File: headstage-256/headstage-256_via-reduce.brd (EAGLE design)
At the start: 32 x 32 mm, 291 parts, among them J2 MMCX-J-P-H-ST-SM1/U.FL-R-SMT(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, J4 PINHD-2X5+4DF40-HEAD, J5 5041940270, U1 OPA170, U10 NRF24L01QFN, U11 CAT4016_QFN, U12 CAT4016_QFN, U13 TPL0501_UQFN, U14 TPL0501_UQFN, U15 MICROSD_473093751, U16 10M08SAM15317G, U17 Si8487DB, U18 MAX17048_WLP, U19 BNO055, U2 OPA170, U20 TPS61202, U21 RHD2064_BGA, U22 RHD2064_BGA, U23 TS4231, U24 TS4231, U25 LT3463, U26 ASCO-50.000MHZ-EK-T3, U27 TS4231, U28 TLV70733, U29 TS4231, U3 INA826, U30 RHD2064_BGA, U31 RHD2064_BGA, U32 MIC23150, U33 TS4231, U34 TS4231, U35 TPS8268180, U4 INA826, U5 DAC5311, U6 DAC5311, U7 DS90UB913A_WQFN, U8 ADG1401, U9 ADG1401, Y1 FW1600008, Y2 ECS-.327-12.5-1210-TR

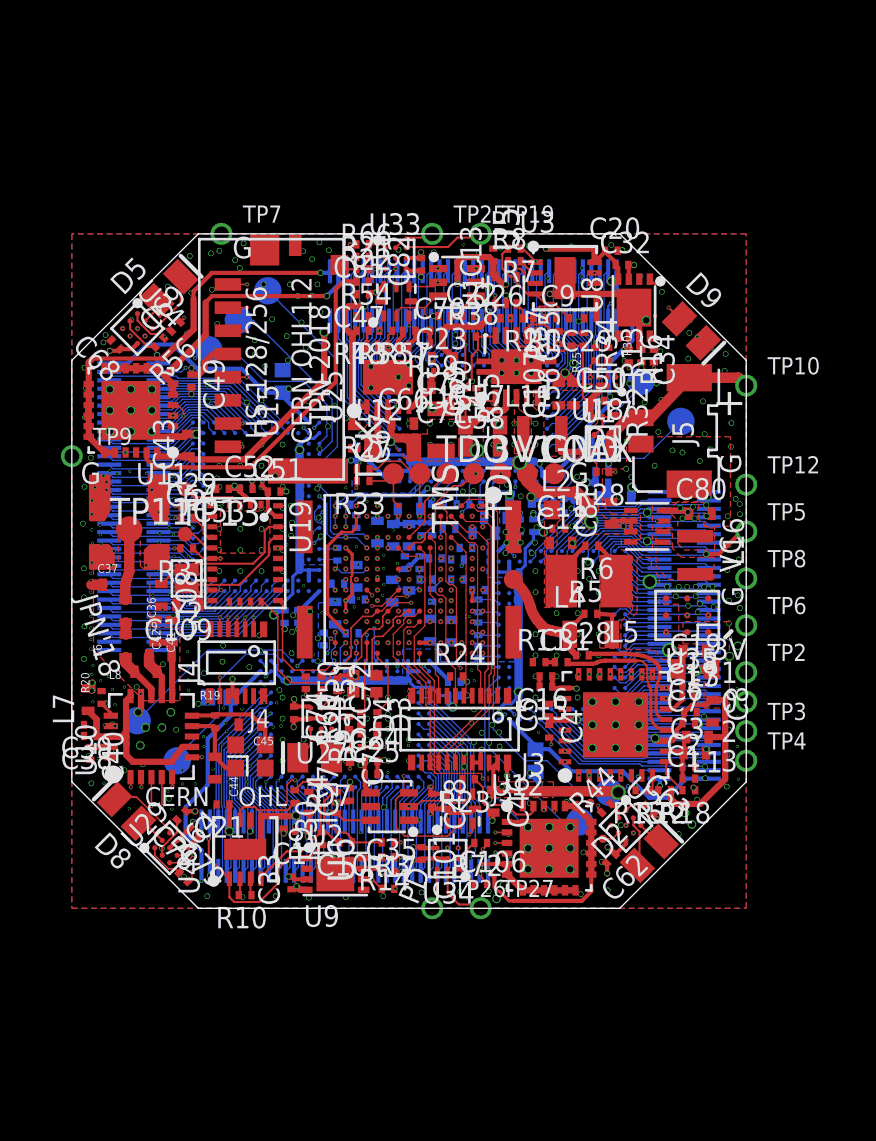
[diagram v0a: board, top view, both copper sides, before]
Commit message: Updates due to production questions from speedy
- Space added between some components
- 3.3V stub removed from headstage-64
- Intan AUXOUTs routed to test points on both boards
- Crystal's re-routed to drive FPGA clock pins that interface with an
avaialble PLL. Previous routing went to clock pins that had no PLL on
both designs.
- Some pins swapping to simplfy routing on both boards.
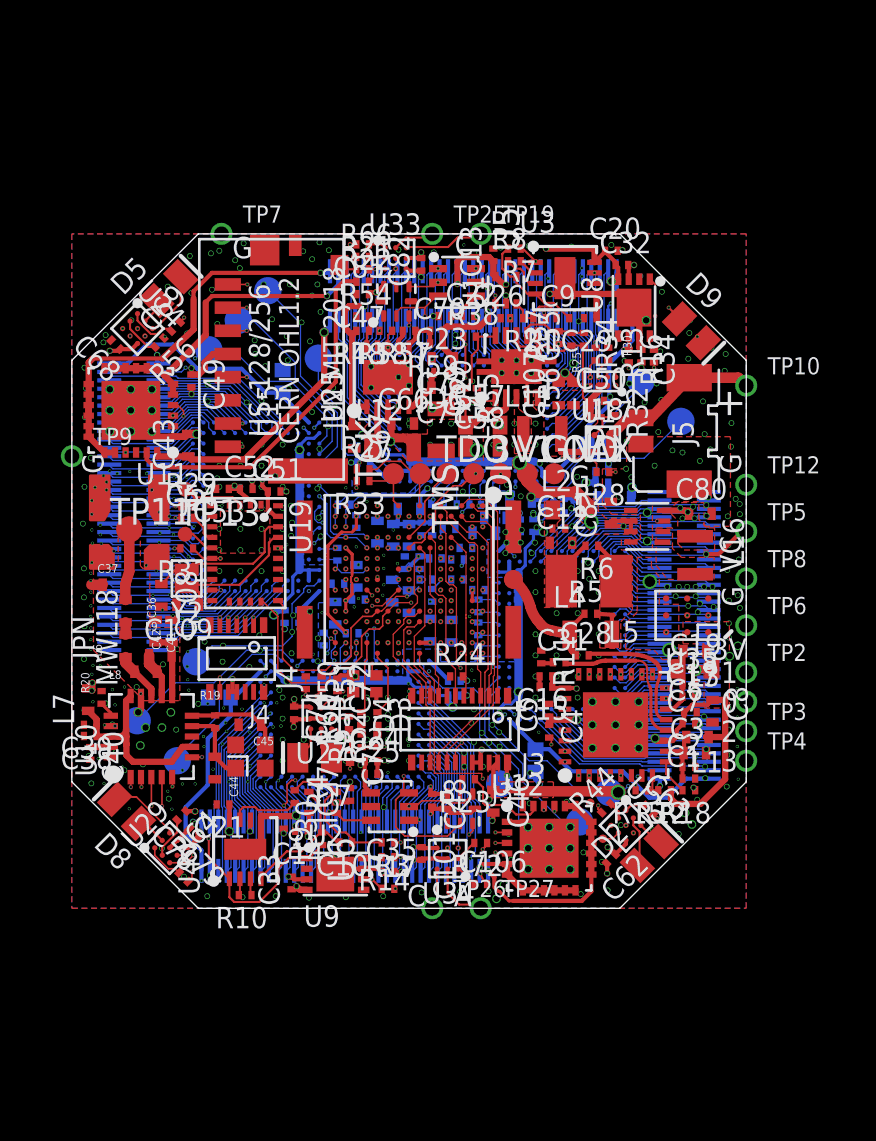
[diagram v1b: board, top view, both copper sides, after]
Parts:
- added TP30, TP31, TP32: (no value), jonnew:TP13R
- moved R11 0.27 mm to (6.28, -4.08), turned to 270 degrees
- moved J4 0.20 mm to (-8.18, -4.15)
- moved C31 0.10 mm to (7.12, -4.33)
- moved C60 0.10 mm to (-2.15, 5.16)
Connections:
- new net N$23: TP30.TP, U21.N16
- new net N$32: TP32.TP, U30.N16
- new net N$40: TP31.TP, U22.N16
- net N$22: now also U16.J5; no longer U16.H11
- net STIM_NULL_A: now also U16.H11; no longer U16.J5
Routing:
- net N$40: track 0.00 -> 8.44 mm
- net N$32: track 0.00 -> 8.41 mm
- net N$23: track 0.00 -> 8.38 mm
- net N$22: track 4.27 -> 6.70 mm, vias 0 -> 2
- net STIM_NULL_A: track 20.9 -> 22.7 mm
- net AGND: track 8.45 -> 8.09 mm, vias 266 -> 273
- added copper zone on layer 1, net N$22
- added copper zone on layer 2, net N$22
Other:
- board text added: "(C) JPN"
- board text added: "HS-128/256"
- board text added: "Headstage-256"
- board text added: "JPN MIT 2018"
- board text added: "JPN MWL18"
- board text added: "OUT"
- board text removed: "CERN"
- board text removed: "HS-128/256 JPN 2018"
- board text removed: "JPN'18"
- board text removed: "JPN, MIT"
- board text removed: "OHL"
- board text removed: "PD"
- board text removed: "headstage-256"

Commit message: Added AGND testpoints to bottom of headstage-64 and headstage-256
- So that people can actually use the other IO test points...
- These are ready for production
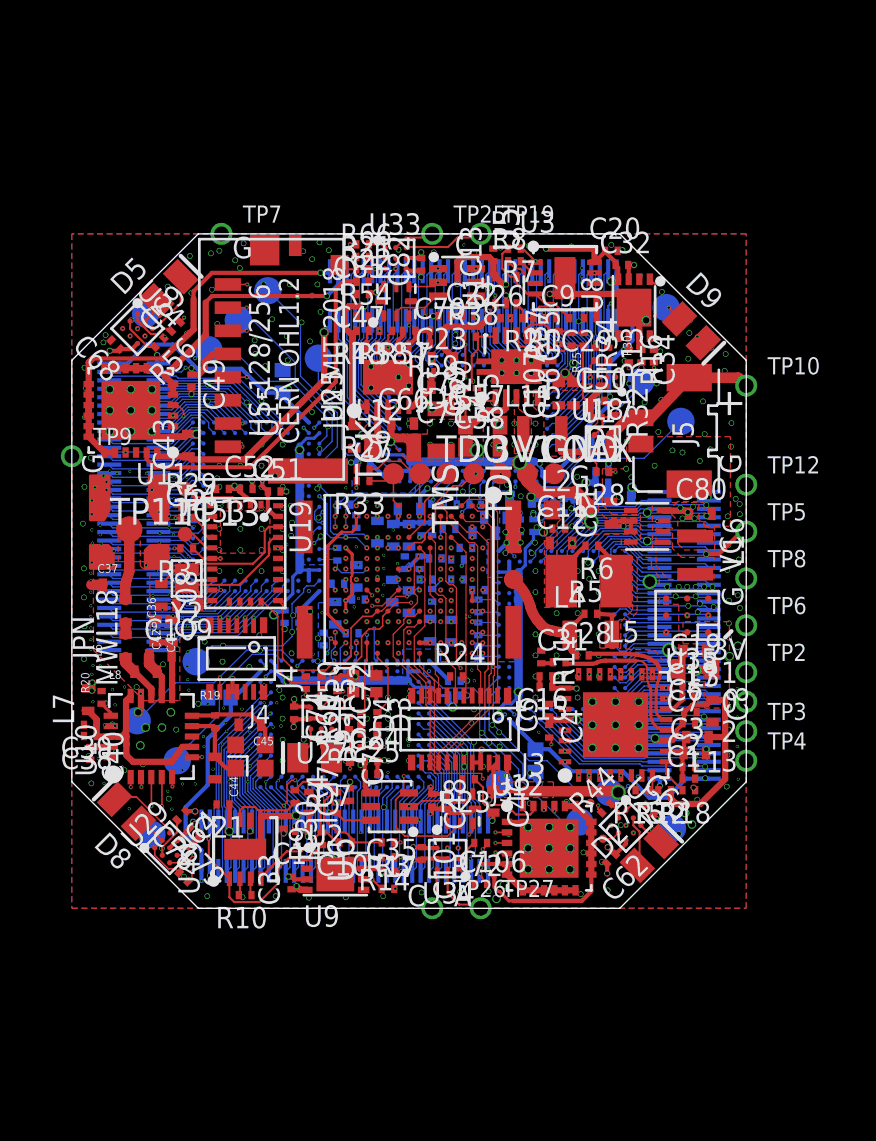
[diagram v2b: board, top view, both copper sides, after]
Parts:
- added TP33, TP34, TP35, TP36: (no value), jonnew:TP13R
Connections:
- net AGND: now also TP33.TP, TP34.TP, TP35.TP, TP36.TP
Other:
- board text added: "AG"
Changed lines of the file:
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@@
 <setting verticaltext="up"/>
 </settings>
-<grid distance="0.1" unitdist="mm" unit="mm" style="lines" multiple="1" display="yes" altdistance="0.025" altunitdist="inch" altunit="inch"/>
+<grid distance="0.25" unitdist="mm" unit="mm" style="lines" multiple="1" display="yes" altdistance="0.025" altunitdist="inch" altunit="inch"/>
 <layers>
 <layer number="1" name="Top" color="4" fill="1" visible="yes" active="yes"/>
@@
 <text x="-14.9" y="-3.15" size="1.016" layer="21" font="vector" ratio="18" distance="10" rot="R90" align="center">JPN
 MWL18</text>
-<text x="-6.05" y="11.4" size="1.016" layer="22" font="vector" ratio="18" rot="MR225" align="center">OUT</text>
-<text x="-11.4" y="-6.05" size="1.016" layer="22" font="vector" ratio="18" rot="MR135" align="center">OUT</text>
-<text x="6.05" y="-11.4" size="1.016" layer="22" font="vector" ratio="18" rot="SMR225" align="center">OUT</text>
+<text x="-11.3" y="-5.6" size="1.016" layer="22" font="vector" ratio="18" rot="SMR135" align="center">OUT</text>
+<text x="-11.4" y="-11" size="1.016" layer="22" font="vector" ratio="18" rot="SMR135" align="center">AG</text>
+<text x="5.6" y="-11.3" size="1.016" layer="22" font="vector" ratio="18" rot="SMR45" align="center">OUT</text>
+<text x="11.25" y="-11.65" size="1.016" layer="22" font="vector" ratio="18" rot="SMR45" align="center">G</text>
+<text x="11.3" y="5.6" size="1.016" layer="22" font="vector" ratio="18" rot="SMR315" align="center">OUT</text>
+<text x="11.4" y="11" size="1.016" layer="22" font="vector" ratio="18" rot="SMR315" align="center">AG</text>
+<text x="-5.6" y="11.3" size="1.016" layer="22" font="vector" ratio="18" rot="SMR225" align="center">OUT</text>
+<text x="-11.25" y="11.65" size="1.016" layer="22" font="vector" ratio="18" rot="SMR225" align="center">G</text>
 </plain>
 <attributes>
@@
 <element name="TP32" library="jonnew" package="TP13R" value="" x="4.3" y="-10.1" rot="MR0">
 <attribute name="TP_SIGNAL_NAME" value="" x="4.3" y="-10.1" size="1.778" layer="28" rot="MR0" display="off"/>
+</element>
+<element name="TP33" library="jonnew" package="TP13R" value="" x="-12.2" y="-12.5" rot="MR0">
+<attribute name="TP_SIGNAL_NAME" value="" x="-12.2" y="-12.5" size="1.778" layer="28" rot="MR0" display="off"/>
+</element>
+<element name="TP34" library="jonnew" package="TP13R" value="" x="12.5" y="-12.2" rot="MR0">
+<attribute name="TP_SIGNAL_NAME" value="" x="12.5" y="-12.2" size="1.778" layer="28" rot="MR0" display="off"/>
+</element>
+<element name="TP35" library="jonnew" package="TP13R" value="" x="12.2" y="12.5" rot="MR0">
+<attribute name="TP_SIGNAL_NAME" value="" x="12.2" y="12.5" size="1.778" layer="28" rot="MR0" display="off"/>
+</element>
+<element name="TP36" library="jonnew" package="TP13R" value="" x="-12.5" y="12.2" rot="MR0">
+<attribute name="TP_SIGNAL_NAME" value="" x="-12.5" y="12.2" size="1.778" layer="28" rot="MR0" display="off"/>
 </element>
 </elements>
@@
 <via x="3.5" y="-9.275" extent="5-16" drill="0.2"/>
 <via x="4.65" y="-11.175" extent="5-16" drill="0.2"/>
+<contactref element="TP33" pad="TP"/>
+<contactref element="TP34" pad="TP"/>
+<contactref element="TP35" pad="TP"/>
+<contactref element="TP36" pad="TP"/>
 <polygon width="0.0508" layer="16" thermals="no">
 <vertex x="3.9246" y="-4.55" curve="180"/>

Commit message: headstage-256 rev 1.1
- Should be ready for speedy
- 8 layer board should fix radio-freq isolation issue on previous
version
- Other small circuit modifications and fixes
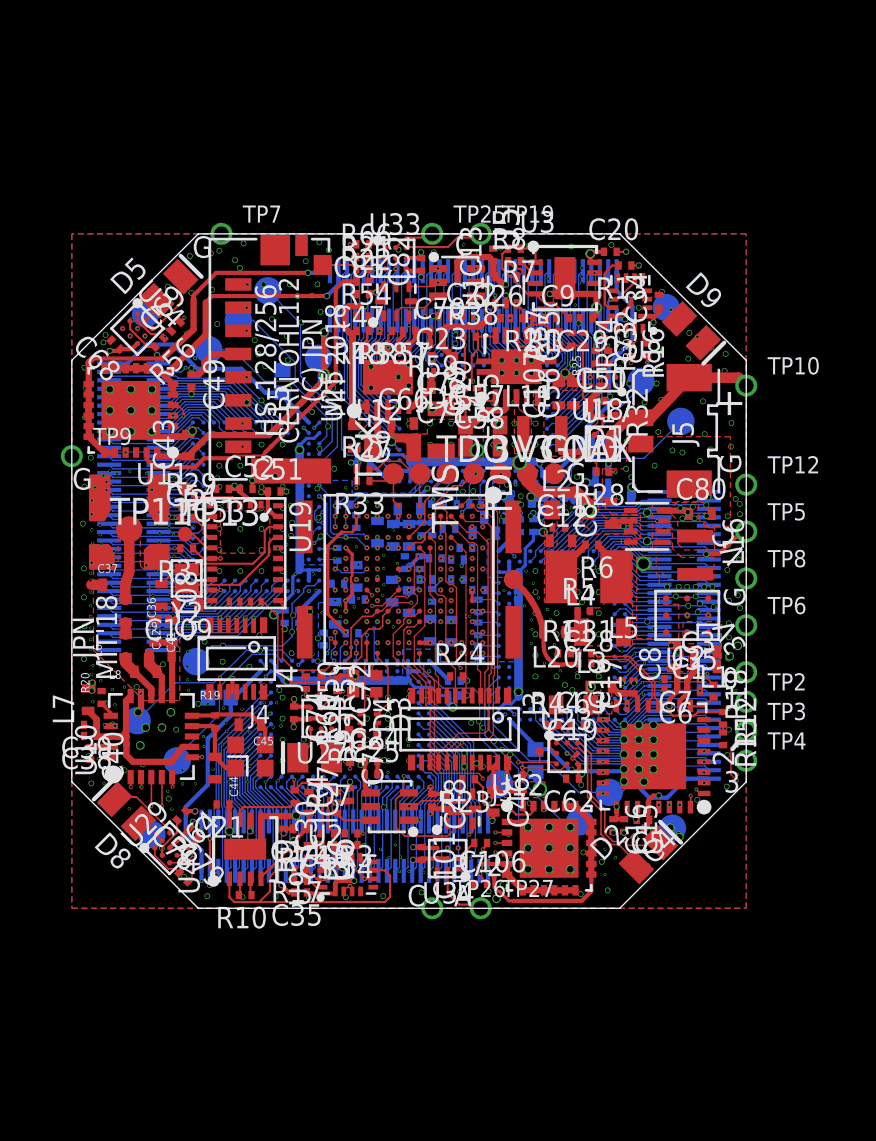
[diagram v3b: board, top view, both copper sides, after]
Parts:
- added L20: BLM15PX121SN1D, jonnew:0402T
- added R73, R74: 10k, jonnew:0201T
- R13, R14: value 49.9 -> 590
- U8, U9: value ADG1401 -> DG509B; device jonnew:LFCSP8-2X3 -> jonnew:MQFN16-1.8X2.6
- moved C16 7.77 mm to (9.70, -12.1), turned to 270 degrees
- moved C15 7.56 mm to (10.2, -12.1), turned to 270 degrees
- moved C5 6.84 mm to (11.1, -11.8), turned to 180 degrees
- moved C4 6.47 mm to (10.9, -12.4), turned to 225 degrees
- moved C19 6.00 mm to (7.80, -6.35), turned to 180 degrees
- moved C63 5.27 mm to (8.00, -7.30), turned to 0 degrees
- moved TP28 4.86 mm to (5.41, -9.66), turned to 45 degrees
- moved R18 4.85 mm to (14.4, -5.69), turned to 270 degrees
- moved L3 4.77 mm to (9.10, -5.50), turned to 0 degrees
- moved R44 4.70 mm to (6.80, -7.30), turned to 0 degrees
- moved R15 4.56 mm to (14.9, -7.96), turned to 270 degrees
- moved R13 4.51 mm to (10.2, 14.5), turned to 180 degrees
- moved U23 4.41 mm to (7.50, -8.65), turned to 0 degrees
- moved R12 4.40 mm to (14.9, -6.99), turned to 270 degrees
- moved C35 4.26 mm to (-5.15, -15.2), turned to 180 degrees
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- renumbered 3V1 to 3V3
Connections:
- net N$44 renamed DOUT_P
- net N$45 renamed DOUT_N
- removed net N$54: C9.1, R1.2, R2.1, U1.3
- removed net N$61: C10.1, R3.2, R4.1, U2.3
- new net ISTIM_A_PRE: R7.1, U3.1, U8.7
- new net ISTIM_B_PRE: R9.1, U4.1, U9.7
- new net ISTIM_MONO_A: C9.1, R1.2, R2.1, U1.3, U21.N5
- new net ISTIM_MONO_B: C10.1, R3.2, R4.1, U2.3, U30.N5
- new net N$31: R73.2, U8.16
- new net N$41: R74.2, U9.16
- new net PREFILT: L20.1, L4.1, R5.1
- net !LIPO_ALRT: now also U16.E7; no longer U16.A2
- net +15V0: now also U8.12, U9.12; no longer U8.4, U9.4
- net +3V3: now also R73.1, R74.1
- net -15V0: now also U8.1, U9.1; no longer U8.7, U8.PAD, U9.7, U9.PAD
- net DIN0: now also U16.B11; no longer U16.D7
- net DIN1: now also U16.B12; no longer U16.B8
- net DIN10: now also U16.B8; no longer U16.B12
- net DIN11: now also U16.B7; no longer U16.D11
- net DIN2: now also U16.D11; no longer U16.C8
- net DIN3: now also U16.A13; no longer U16.A9
- net DIN4: now also U16.B13; no longer U16.E7
- net DIN5: now also U16.A14; no longer U16.E9
- net DIN6: now also U16.B14; no longer U16.D10
- net DIN7: now also U16.B15; no longer U16.E10
- net DIN8: now also U16.A9; no longer U16.A11
- net DIN9: now also U16.A7; no longer U16.B11
- net GND: now also U8.13, U8.14, U8.2, U9.13, U9.14, U9.2; no longer U8.3
- net HSYNC: now also U16.A5; no longer U16.A13
- net ISTIM_A: now also U8.10, U8.6; no longer R7.1, U3.1, U8.1
- net ISTIM_B: now also U9.10, U9.6; no longer R9.1, U4.1, U9.1
- net LIPO_QSTRT: now also U16.A2; no longer U16.A3
- net N$55: now also U8.11; no longer U8.8
- net N$62: now also U9.11; no longer U9.8
- net PCLK: now also U16.C8; no longer U16.A14
- net SERDES_EN: now also U16.D7; no longer U16.B4
- net SERDES_GPIO0: now also U16.E9; no longer U16.B6
- net SERDES_GPIO1: now also U16.D10; no longer U16.A5
- net SERDES_GPIO2: now also U16.E10; no longer U16.B7
- net SERDES_GPIO3: now also U16.A11; no longer U16.A7
- net SERDES_SCL: now also U16.B4; no longer U16.B14
- net SERDES_SDA: now also U16.B6; no longer U16.B15
- net SIGOUT: now also L20.2; no longer L4.1, R5.1
- net STIM_NULL_A: now also U8.15; no longer U8.6
- net STIM_NULL_B: now also U9.15; no longer U9.6
- net VDAC_A: no longer U21.N5
- net VDAC_B: no longer U30.N5
- net VSYNC: now also U16.A3; no longer U16.B13
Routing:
- net ISTIM_MONO_A: track 0.00 -> 15.3 mm, vias 0 -> 4
- net ISTIM_B_PRE: track 0.00 -> 14.3 mm
- net VDAC_A: track 15.0 -> 2.33 mm, vias 5 -> 2
- net ISTIM_MONO_B: track 0.00 -> 11.6 mm, vias 0 -> 2
- net PCLK: track 10.5 -> 22.0 mm
- net VDAC_B: track 13.5 -> 2.23 mm, vias 4 -> 0
- net SERDES_GPIO0: track 16.4 -> 27.1 mm
- net DIN10: track 8.70 -> 19.3 mm
- net DIN8: track 7.88 -> 18.2 mm
- net VSYNC: track 10.6 -> 20.0 mm
- net DIN9: track 8.65 -> 17.9 mm
- net DIN11: track 10.3 -> 19.5 mm
- net HSYNC: track 9.30 -> 18.4 mm
- net SERDES_GPIO1: track 16.4 -> 25.3 mm
- net ISTIM_A: track 11.1 -> 2.72 mm, vias 3 -> 1
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- added copper zone on layer 3, net !IMU_RESET
- added copper zone on layer 3, net !LIPO_ALRT
- added copper zone on layer 3, net +15V0
- added copper zone on layer 5, net +15V0
- added copper zone on layer 3, net +1V8
- added copper zone on layer 5, net +1V8
- added copper zone on layer 5, net +3V3
- added copper zone on layer 3, net -15V0
- added copper zone on layer 5, net -15V0
- added copper zone on layer 7, net AGND
- added copper zone on layer 7, net AUXIN1_C
- added copper zone on layer 7, net AUXIN1_D
- added copper zone on layer 3, net DAC_A_CS
- added copper zone on layer 3, net DAC_B_CS
- added copper zone on layer 3, net DIN0
- added copper zone on layer 3, net DIN1
- added copper zone on layer 1, net DIN10
- added copper zone on layer 3, net DIN10
- added copper zone on layer 1, net DIN11
- added copper zone on layer 3, net DIN11
- added copper zone on layer 3, net DIN2
- added copper zone on layer 3, net DIN3
- added copper zone on layer 3, net DIN4
- added copper zone on layer 3, net DIN5
- added copper zone on layer 3, net DIN6
- added copper zone on layer 3, net DIN7
- added copper zone on layer 1, net DIN8
- added copper zone on layer 3, net DIN8
- added copper zone on layer 1, net DIN9
- added copper zone on layer 3, net DIN9
- added copper zone on layer 3, net ESTIM_POW_EN
- added copper zone on layer 3, net EXP10
- added copper zone on layer 3, net EXP11
- added copper zone on layer 3, net EXP12
- added copper zone on layer 3, net EXP13
- added copper zone on layer 3, net EXP14
- added copper zone on layer 3, net EXP8
- added copper zone on layer 3, net EXP9
- added copper zone on layer 2, net GND
- added copper zone on layer 4, net GND
- added copper zone on layer 6, net GND
- added copper zone on layer 7, net GND
- added copper zone on layer 1, net HSYNC
- added copper zone on layer 3, net HSYNC
- added copper zone on layer 3, net IMU_INT
- added copper zone on layer 7, net INTAN_EN
- added copper zone on layer 7, net INTAN_VDD
- added copper zone on layer 1, net ISTIM_A_PRE
- added copper zone on layer 3, net ISTIM_A_PRE
- added copper zone on layer 3, net ISTIM_B
- added copper zone on layer 1, net ISTIM_MONO_A
- added copper zone on layer 16, net ISTIM_MONO_A
- added copper zone on layer 3, net ISTIM_MONO_A
- added copper zone on layer 1, net ISTIM_MONO_B
- added copper zone on layer 16, net ISTIM_MONO_B
- added copper zone on layer 3, net ISTIM_MONO_B
- added copper zone on layer 3, net LED_BLANK
- added copper zone on layer 3, net LED_CLK
- added copper zone on layer 3, net LED_LATCH
- added copper zone on layer 3, net LED_SIN
- added copper zone on layer 3, net LH_DATA1
- added copper zone on layer 3, net LH_DATA2
- added copper zone on layer 3, net LH_DATA3
- added copper zone on layer 3, net LH_DATA4
- added copper zone on layer 3, net LH_DATA5
- added copper zone on layer 3, net LH_DATA6
- added copper zone on layer 3, net LH_ENV1
- added copper zone on layer 3, net LH_ENV2
- added copper zone on layer 3, net LH_ENV3
- added copper zone on layer 3, net LH_ENV4
- added copper zone on layer 3, net LH_ENV5
- added copper zone on layer 3, net LH_ENV6
- added copper zone on layer 3, net LIPO_QSTRT
- added copper zone on layer 3, net MISO
- added copper zone on layer 3, net MOSI
- added copper zone on layer 5, net N$10
- added copper zone on layer 3, net N$22
- added copper zone on layer 1, net N$50
- added copper zone on layer 5, net N$69
- added copper zone on layer 3, net N$70
- added copper zone on layer 3, net N$97
- added copper zone on layer 3, net N$98
- added copper zone on layer 3, net NRF_CS
- added copper zone on layer 3, net NRF_EN
- added copper zone on layer 3, net NRF_IRQ
- added copper zone on layer 3, net PCLK
- added copper zone on layer 3, net POTA_CS
- added copper zone on layer 3, net POTB_CS
- added copper zone on layer 7, net RHD_CLK+_AC
- added copper zone on layer 7, net RHD_CLK+_BD
- added copper zone on layer 7, net RHD_CLK-_AC
- added copper zone on layer 7, net RHD_CLK-_BD
- added copper zone on layer 7, net RHD_CS+_AC
- added copper zone on layer 7, net RHD_CS+_BD
- added copper zone on layer 7, net RHD_CS-_AC
- added copper zone on layer 7, net RHD_CS-_BD
- added copper zone on layer 7, net RHD_MISO+_B
- added copper zone on layer 7, net RHD_MISO+_D
- added copper zone on layer 7, net RHD_MISO-_B
- added copper zone on layer 7, net RHD_MISO-_C
- added copper zone on layer 7, net RHD_MISO-_D
- added copper zone on layer 7, net RHD_MOSI+_AC
- added copper zone on layer 7, net RHD_MOSI+_BD
- added copper zone on layer 7, net RHD_MOSI-_AC
- added copper zone on layer 7, net RHD_MOSI-_BD
- added copper zone on layer 3, net SCL
- added copper zone on layer 3, net SCLK
- added copper zone on layer 3, net SDA
- added copper zone on layer 3, net SD_CS
- added copper zone on layer 3, net SD_DAT2
- added copper zone on layer 3, net SD_IRQ
- added copper zone on layer 3, net SD_MISO
- added copper zone on layer 3, net SD_MOSI
- added copper zone on layer 3, net SD_SCLK
- added copper zone on layer 3, net SERDES_EN
- added copper zone on layer 1, net SERDES_GPIO0
- added copper zone on layer 3, net SERDES_GPIO0
- added copper zone on layer 3, net SERDES_GPIO1
- added copper zone on layer 1, net SERDES_GPIO2
- added copper zone on layer 3, net SERDES_GPIO2
- added copper zone on layer 3, net SERDES_GPIO3
- added copper zone on layer 3, net SERDES_SCL
- added copper zone on layer 3, net SERDES_SDA
- added copper zone on layer 3, net STIM_NULL_A
- added copper zone on layer 3, net STIM_NULL_B
- added copper zone on layer 3, net TDI
- added copper zone on layer 5, net VCCA
- added copper zone on layer 5, net VCCIO
- added copper zone on layer 3, net VCOAX
- added copper zone on layer 5, net VCOAX
- added copper zone on layer 3, net VDAC_A
- added copper zone on layer 3, net VI_A
- added copper zone on layer 3, net VSYNC
- removed copper zone on layer 2, net !IMU_RESET
- removed copper zone on layer 2, net !LIPO_ALRT
- removed copper zone on layer 2, net +15V0
- removed copper zone on layer 4, net +15V0
- removed copper zone on layer 2, net +1V8
- removed copper zone on layer 4, net +3V3
- removed copper zone on layer 2, net -15V0
- removed copper zone on layer 4, net -15V0
- removed copper zone on layer 5, net AGND
- removed copper zone on layer 5, net AUXIN1_C
- removed copper zone on layer 5, net AUXIN1_D
- removed copper zone on layer 2, net DAC_A_CS
- removed copper zone on layer 2, net DAC_B_CS
- removed copper zone on layer 2, net DIN0
- removed copper zone on layer 2, net DIN1
- removed copper zone on layer 2, net DIN10
- removed copper zone on layer 2, net DIN11
- removed copper zone on layer 2, net DIN2
- removed copper zone on layer 2, net DIN3
- removed copper zone on layer 2, net DIN4
- removed copper zone on layer 2, net DIN5
- removed copper zone on layer 2, net DIN6
- removed copper zone on layer 2, net DIN7
- removed copper zone on layer 2, net DIN8
- removed copper zone on layer 2, net DIN9
- removed copper zone on layer 2, net ESTIM_POW_EN
- removed copper zone on layer 2, net EXP10
- removed copper zone on layer 2, net EXP11
- removed copper zone on layer 2, net EXP12
- removed copper zone on layer 2, net EXP13
- removed copper zone on layer 2, net EXP14
- removed copper zone on layer 2, net EXP8
- removed copper zone on layer 2, net EXP9
- removed copper zone on layer 3, net GND
- removed copper zone on layer 5, net GND
- removed copper zone on layer 2, net HSYNC
- removed copper zone on layer 2, net IMU_INT
- removed copper zone on layer 5, net INTAN_EN
- removed copper zone on layer 5, net INTAN_VDD
- removed copper zone on layer 2, net ISTIM_A
- removed copper zone on layer 2, net LED_BLANK
- removed copper zone on layer 2, net LED_CLK
- removed copper zone on layer 2, net LED_LATCH
- removed copper zone on layer 2, net LED_SIN
- removed copper zone on layer 2, net LH_DATA1
- removed copper zone on layer 2, net LH_DATA2
- removed copper zone on layer 2, net LH_DATA3
- removed copper zone on layer 2, net LH_DATA4
- removed copper zone on layer 2, net LH_DATA5
- removed copper zone on layer 2, net LH_DATA6
- removed copper zone on layer 2, net LH_ENV1
- removed copper zone on layer 2, net LH_ENV2
- removed copper zone on layer 2, net LH_ENV3
- removed copper zone on layer 2, net LH_ENV4
- removed copper zone on layer 2, net LH_ENV5
- removed copper zone on layer 2, net LH_ENV6
- removed copper zone on layer 2, net LIPO_QSTRT
- removed copper zone on layer 2, net MISO
- removed copper zone on layer 2, net MOSI
- removed copper zone on layer 4, net N$10
- removed copper zone on layer 2, net N$22
- removed copper zone on layer 2, net N$69
- removed copper zone on layer 4, net N$69
- removed copper zone on layer 2, net N$70
- removed copper zone on layer 2, net N$97
- removed copper zone on layer 2, net N$98
- removed copper zone on layer 2, net NRF_CS
- removed copper zone on layer 2, net NRF_EN
- removed copper zone on layer 2, net NRF_IRQ
- removed copper zone on layer 2, net PCLK
- removed copper zone on layer 2, net POTA_CS
- removed copper zone on layer 2, net POTB_CS
- removed copper zone on layer 5, net RHD_CLK+_AC
- removed copper zone on layer 5, net RHD_CLK+_BD
- removed copper zone on layer 5, net RHD_CLK-_AC
- removed copper zone on layer 5, net RHD_CLK-_BD
- removed copper zone on layer 5, net RHD_CS+_AC
- removed copper zone on layer 5, net RHD_CS+_BD
- removed copper zone on layer 5, net RHD_CS-_AC
- removed copper zone on layer 5, net RHD_CS-_BD
- removed copper zone on layer 5, net RHD_MISO+_B
- removed copper zone on layer 5, net RHD_MISO+_D
- removed copper zone on layer 5, net RHD_MISO-_B
- removed copper zone on layer 5, net RHD_MISO-_C
- removed copper zone on layer 5, net RHD_MISO-_D
- removed copper zone on layer 5, net RHD_MOSI+_AC
- removed copper zone on layer 5, net RHD_MOSI+_BD
- removed copper zone on layer 5, net RHD_MOSI-_AC
- removed copper zone on layer 5, net RHD_MOSI-_BD
- removed copper zone on layer 2, net SCL
- removed copper zone on layer 2, net SCLK
- removed copper zone on layer 2, net SDA
- removed copper zone on layer 2, net SD_CS
- removed copper zone on layer 2, net SD_DAT2
- removed copper zone on layer 2, net SD_IRQ
- removed copper zone on layer 2, net SD_MISO
- removed copper zone on layer 2, net SD_MOSI
- removed copper zone on layer 2, net SD_SCLK
- removed copper zone on layer 2, net SERDES_EN
- removed copper zone on layer 2, net SERDES_GPIO0
- removed copper zone on layer 2, net SERDES_GPIO1
- removed copper zone on layer 2, net SERDES_GPIO2
- removed copper zone on layer 2, net SERDES_GPIO3
- removed copper zone on layer 2, net SERDES_SCL
- removed copper zone on layer 2, net SERDES_SDA
- removed copper zone on layer 2, net STIM_NULL_A
- removed copper zone on layer 2, net STIM_NULL_B
- removed copper zone on layer 2, net TDI
- removed copper zone on layer 4, net VCCA
- removed copper zone on layer 4, net VCCIO
- removed copper zone on layer 2, net VCOAX
- removed copper zone on layer 4, net VCOAX
- removed copper zone on layer 16, net VDAC_A
- removed copper zone on layer 2, net VDAC_A
- removed copper zone on layer 1, net VDAC_B
- removed copper zone on layer 16, net VDAC_B
- removed copper zone on layer 2, net VDAC_B
- removed copper zone on layer 2, net VI_A
- removed copper zone on layer 2, net VSYNC
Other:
- board text added: "(C)JPN"
- board text added: "JPN MIT'18"
- board text added: "MIT 2018"
- board text added: "r1.1"
- board text removed: "JPN MIT 2018"
- board text removed: "JPN MWL18"
- board text removed: "r1.0"

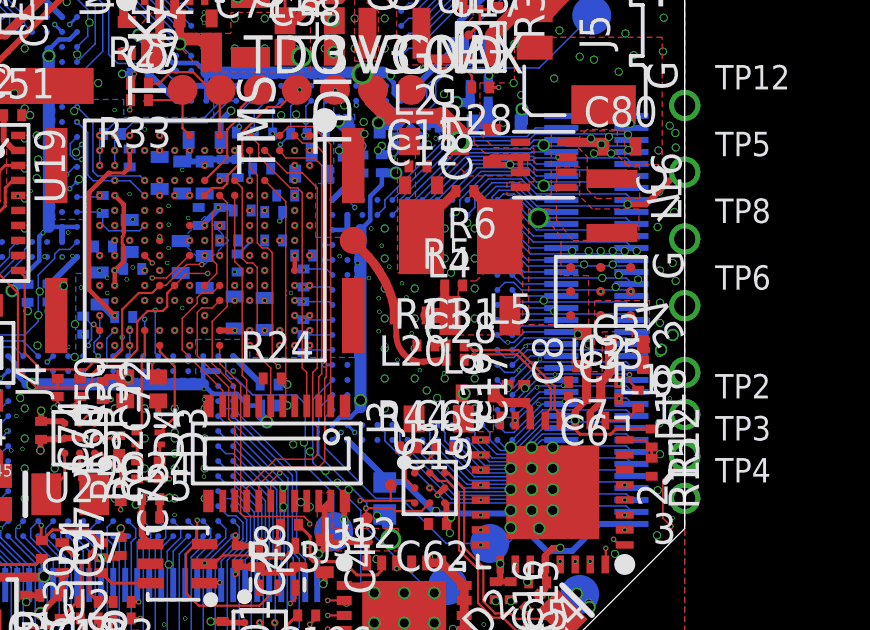
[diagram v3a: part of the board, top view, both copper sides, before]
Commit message: Minore changes to headstage-256
- But restrict layer on top around high frequency lines to widen out
spacing to top level ground layer. Provides more accurate micro-strip
characteristics.
- Gerbers updated.
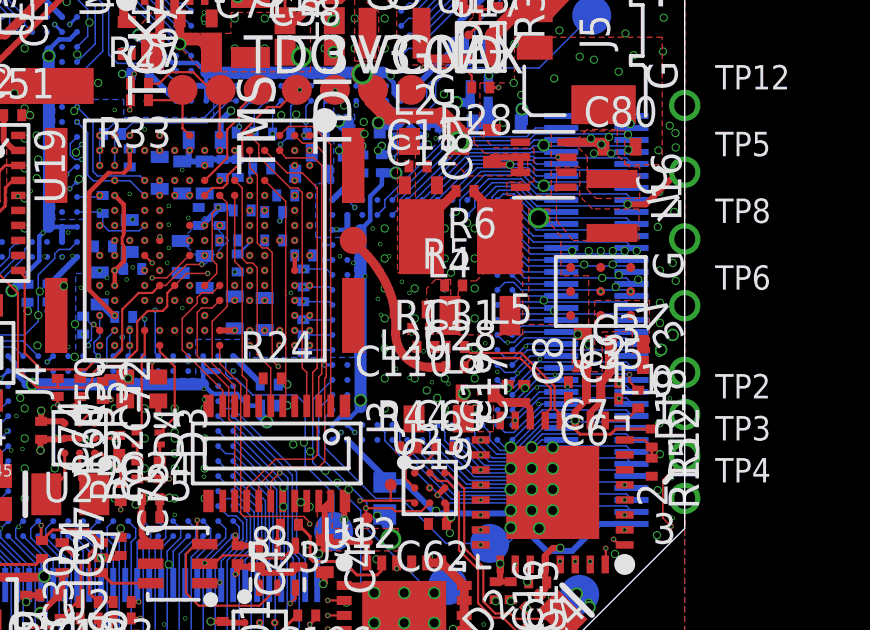
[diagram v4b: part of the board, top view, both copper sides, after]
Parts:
- added C110: 68pF, NP0 (DNP), jonnew:0201T
- moved C28 0.25 mm to (8.35, -4.62)
- moved L20 0.20 mm to (6.90, -2.70)
- moved C31 0.05 mm to (8.35, -3.95)
- moved R11 0.05 mm to (7.38, -3.95)
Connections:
- net GND: now also C110.2
- net PREFILT: now also C110.1
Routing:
- net PREFILT: track 1.81 -> 0.25 mm
- net GND: vias 450 -> 451
- added copper zone on layer 1, net PREFILT
